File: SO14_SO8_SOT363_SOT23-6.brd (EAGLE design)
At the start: 34 parts

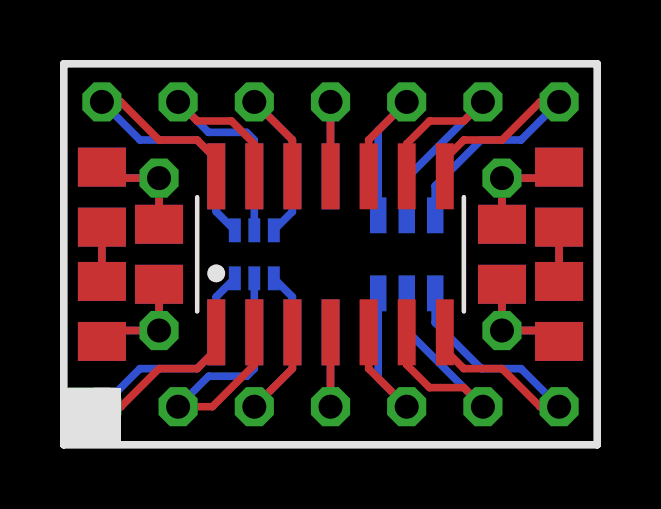
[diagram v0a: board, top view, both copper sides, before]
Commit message: adjusted trace widths
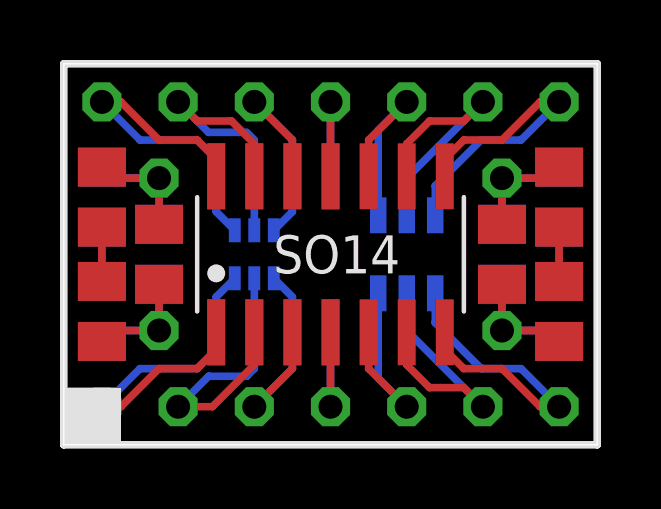
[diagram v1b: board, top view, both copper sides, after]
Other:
- board outline added: 17.8 x 12.7 mm
- board text added: "SO14"
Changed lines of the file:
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@@
 <grid distance="0.05" unitdist="inch" unit="mm" style="lines" multiple="1" display="yes" altdistance="0.025" altunitdist="inch" altunit="mm"/>
 <layers>
-<layer number="1" name="Top" color="4" fill="1" visible="yes" active="yes"/>
+<layer number="1" name="Top" color="4" fill="1" visible="no" active="yes"/>
 <layer number="2" name="Route2" color="1" fill="3" visible="no" active="no"/>
 <layer number="3" name="Route3" color="4" fill="3" visible="no" active="no"/>
@@
 <layer number="19" name="Unrouted" color="6" fill="1" visible="yes" active="yes"/>
 <layer number="20" name="Dimension" color="15" fill="1" visible="yes" active="yes"/>
-<layer number="21" name="tPlace" color="7" fill="1" visible="yes" active="yes"/>
+<layer number="21" name="tPlace" color="7" fill="1" visible="no" active="yes"/>
 <layer number="22" name="bPlace" color="7" fill="1" visible="yes" active="yes"/>
-<layer number="23" name="tOrigins" color="15" fill="1" visible="yes" active="yes"/>
+<layer number="23" name="tOrigins" color="15" fill="1" visible="no" active="yes"/>
 <layer number="24" name="bOrigins" color="15" fill="1" visible="yes" active="yes"/>
-<layer number="25" name="tNames" color="7" fill="1" visible="yes" active="yes"/>
+<layer number="25" name="tNames" color="7" fill="1" visible="no" active="yes"/>
 <layer number="26" name="bNames" color="7" fill="1" visible="yes" active="yes"/>
-<layer number="27" name="tValues" color="7" fill="1" visible="yes" active="yes"/>
-<layer number="28" name="bValues" color="7" fill="1" visible="yes" active="yes"/>
+<layer number="27" name="tValues" color="7" fill="1" visible="no" active="yes"/>
+<layer number="28" name="bValues" color="7" fill="1" visible="no" active="yes"/>
 <layer number="29" name="tStop" color="7" fill="3" visible="no" active="yes"/>
-<layer number="30" name="bStop" color="7" fill="6" visible="no" active="yes"/>
+<layer number="30" name="bStop" color="7" fill="6" visible="yes" active="yes"/>
 <layer number="31" name="tCream" color="7" fill="4" visible="no" active="yes"/>
 <layer number="32" name="bCream" color="7" fill="5" visible="no" active="yes"/>
@@
 <layer number="37" name="tTest" color="7" fill="1" visible="no" active="yes"/>
 <layer number="38" name="bTest" color="7" fill="1" visible="no" active="yes"/>
-<layer number="39" name="tKeepout" color="4" fill="11" visible="yes" active="yes"/>
+<layer number="39" name="tKeepout" color="4" fill="11" visible="no" active="yes"/>
 <layer number="40" name="bKeepout" color="1" fill="11" visible="yes" active="yes"/>
-<layer number="41" name="tRestrict" color="4" fill="10" visible="yes" active="yes"/>
+<layer number="41" name="tRestrict" color="4" fill="10" visible="no" active="yes"/>
 <layer number="42" name="bRestrict" color="1" fill="10" visible="yes" active="yes"/>
 <layer number="43" name="vRestrict" color="2" fill="10" visible="yes" active="yes"/>
 <layer number="44" name="Drills" color="7" fill="1" visible="no" active="yes"/>
 <layer number="45" name="Holes" color="7" fill="1" visible="no" active="yes"/>
-<layer number="46" name="Milling" color="3" fill="1" visible="no" active="yes"/>
+<layer number="46" name="Milling" color="3" fill="1" visible="yes" active="yes"/>
 <layer number="47" name="Measures" color="7" fill="1" visible="no" active="yes"/>
-<layer number="48" name="Document" color="7" fill="1" visible="yes" active="yes"/>
-<layer number="49" name="Reference" color="7" fill="1" visible="yes" active="yes"/>
-<layer number="51" name="tDocu" color="7" fill="1" visible="yes" active="yes"/>
-<layer number="52" name="bDocu" color="7" fill="1" visible="yes" active="yes"/>
+<layer number="48" name="Document" color="7" fill="1" visible="no" active="yes"/>
+<layer number="49" name="Reference" color="7" fill="1" visible="no" active="yes"/>
+<layer number="51" name="tDocu" color="7" fill="1" visible="no" active="yes"/>
+<layer number="52" name="bDocu" color="7" fill="1" visible="no" active="yes"/>
 <layer number="91" name="Nets" color="2" fill="1" visible="no" active="no"/>
 <layer number="92" name="Busses" color="1" fill="1" visible="no" active="no"/>
@@
 <layer number="97" name="Info" color="7" fill="1" visible="no" active="no"/>
 <layer number="98" name="Guide" color="6" fill="1" visible="no" active="no"/>
-<layer number="125" name="_tNames" color="14" fill="1" visible="yes" active="yes"/>
-<layer number="126" name="_bNames" color="5" fill="1" visible="yes" active="yes"/>
+<layer number="125" name="_tNames" color="14" fill="1" visible="no" active="yes"/>
+<layer number="126" name="_bNames" color="5" fill="1" visible="no" active="yes"/>
 <layer number="200" name="200bmp" color="1" fill="10" visible="no" active="no"/>
 </layers>
@@
 <rectangle x1="0" y1="10.16" x2="2.54" y2="12.7" layer="22"/>
 <rectangle x1="15.24" y1="0" x2="17.78" y2="2.54" layer="22"/>
+<text x="6.985" y="5.715" size="1.27" layer="21">SO14</text>
+<wire x1="0" y1="0" x2="17.78" y2="0" width="0" layer="20"/>
+<wire x1="17.78" y1="0" x2="17.78" y2="12.7" width="0" layer="20"/>
+<wire x1="17.78" y1="12.7" x2="0" y2="12.7" width="0" layer="20"/>
+<wire x1="0" y1="12.7" x2="0" y2="0" width="0" layer="20"/>
 </plain>
 <attributes>
